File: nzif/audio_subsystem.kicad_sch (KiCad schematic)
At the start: 24 parts, among them U1201 ADAU1361, U1202 SSM2211S

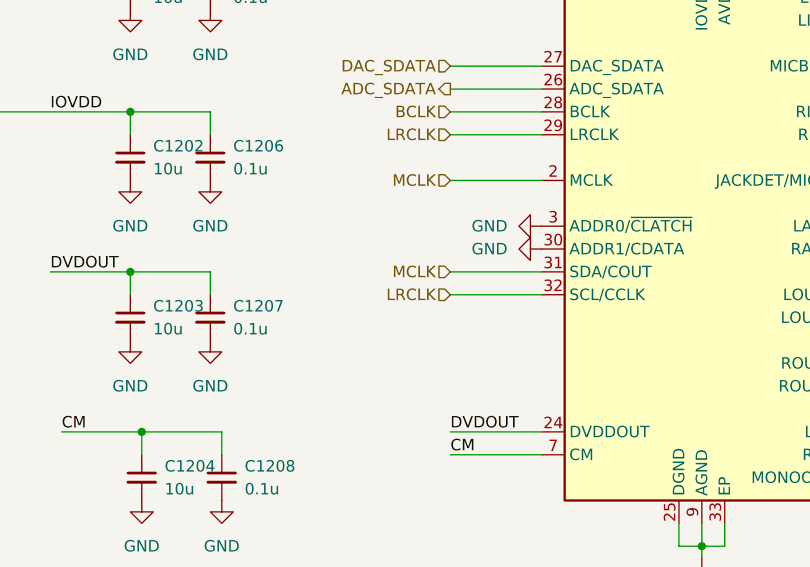
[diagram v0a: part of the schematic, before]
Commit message: top sheet wiring
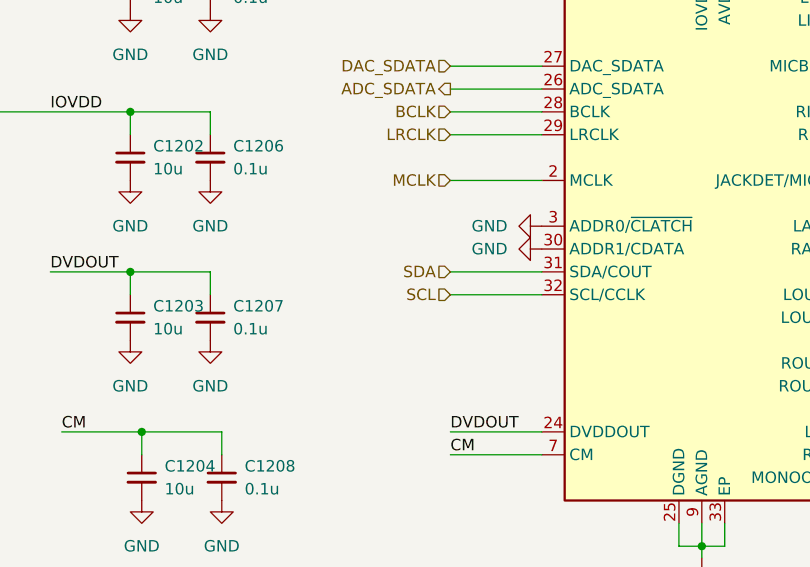
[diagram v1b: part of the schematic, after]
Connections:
- net LRCLK: no longer U1201.32 (SCL/CCLK)
- net MCLK: no longer U1201.31 (SDA/COUT)
- new net SCL: U1201.32 (SCL/CCLK)
- new net SDA: U1201.31 (SDA/COUT)
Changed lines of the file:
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@@
 		)
 	)
-	(hierarchical_label "MCLK"
+	(hierarchical_label "SDA"
 		(shape input)
 		(at 173.99 109.22 180)
@@
 		)
 	)
-	(hierarchical_label "LRCLK"
+	(hierarchical_label "SCL"
 		(shape input)
 		(at 173.99 111.76 180)

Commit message: updated top level
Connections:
- net LOUTN: now also U1201.18 (LOUTP)
- net at C1212.1: no longer U1201.21 (MONOOUT)
- net LOUTP: now reaches U1201.17 (LOUTN)
- net Line_Input_ROUTN: no longer names the net of U1201.16 (ROUTN)
- net Line_Input_ROUTP: no longer names the net of U1201.15 (ROUTP)
- no-connect marks 6 -> 7
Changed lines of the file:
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@@
+	)
+	(junction
+		(at 275.59 81.28)
+		(diameter 0)
+		(color 0 0 0 0)
 	)
 	(junction
@@
 	)
 	(no_connect
+		(at 219.71 121.92)
+	)
+	(no_connect
 		(at 219.71 93.98)
 	)
 	(no_connect
-		(at 219.71 114.3)
+		(at 219.71 132.08)
 	)
 	(no_connect
@@
 	)
 	(no_connect
+		(at 219.71 119.38)
+	)
+	(no_connect
 		(at 219.71 91.44)
 	)
-	(no_connect
-		(at 219.71 111.76)
+	(wire
+		(pts
+			(xy 215.9 180.34) (xy 224.79 180.34)
+		)
+		(stroke
+			(width 0)
+			(type default)
+		)
 	)
 	(wire
@@
 	(wire
 		(pts
-			(xy 219.71 132.08) (xy 227.33 132.08)
-		)
-		(stroke
-			(width 0)
-			(type default)
-		)
-	)
-	(wire
-		(pts
 			(xy 250.19 81.28) (xy 254 81.28)
 		)
@@
 	(wire
 		(pts
-			(xy 219.71 119.38) (xy 224.79 119.38)
+			(xy 219.71 111.76) (xy 228.6 111.76)
 		)
 		(stroke
@@
 	(wire
 		(pts
+			(xy 275.59 81.28) (xy 279.4 81.28)
+		)
+		(stroke
+			(width 0)
+			(type default)
+		)
+	)
+	(wire
+		(pts
+			(xy 215.9 182.88) (xy 224.79 182.88)
+		)
+		(stroke
+			(width 0)
+			(type default)
+		)
+	)
+	(wire
+		(pts
 			(xy 173.99 127) (xy 184.15 127)
 		)
@@
 	(wire
 		(pts
-			(xy 269.24 81.28) (xy 279.4 81.28)
+			(xy 269.24 81.28) (xy 275.59 81.28)
 		)
 		(stroke
@@
 	(wire
 		(pts
-			(xy 227.33 132.08) (xy 227.33 175.26)
-		)
-		(stroke
-			(width 0)
-			(type default)
-		)
-	)
-	(wire
-		(pts
 			(xy 173.99 99.06) (xy 184.15 99.06)
 		)
@@
 	(wire
 		(pts
+			(xy 275.59 76.2) (xy 275.59 81.28)
+		)
+		(stroke
+			(width 0)
+			(type default)
+		)
+	)
+	(wire
+		(pts
 			(xy 173.99 88.9) (xy 184.15 88.9)
 		)
@@
 	(wire
 		(pts
+			(xy 219.71 114.3) (xy 228.6 114.3)
+		)
+		(stroke
+			(width 0)
+			(type default)
+		)
+	)
+	(wire
+		(pts
 			(xy 147.32 93.98) (xy 147.32 91.44)
 		)
@@
 	(wire
 		(pts
-			(xy 219.71 121.92) (xy 224.79 121.92)
-		)
-		(stroke
-			(width 0)
-			(type default)
-		)
-	)
-	(wire
-		(pts
 			(xy 204.47 67.31) (xy 204.47 73.66)
 		)
@@
 	(wire
 		(pts
+			(xy 279.4 76.2) (xy 275.59 76.2)
+		)
+		(stroke
+			(width 0)
+			(type default)
+		)
+	)
+	(wire
+		(pts
 			(xy 254 81.28) (xy 254 83.82)
 		)
@@
 			(width 0)
 			(type default)
+		)
+	)
+	(label "LOUTP"
+		(at 228.6 114.3 180)
+		(effects
+			(font
+				(size 1.27 1.27)
+			)
+			(justify right bottom)
 		)
 	)
@@
 		)
 	)
+	(label "LOUTP"
+		(at 224.79 182.88 180)
+		(effects
+			(font
+				(size 1.27 1.27)
+			)
+			(justify right bottom)
+		)
+	)
 	(label "MICBIAS"
 		(at 232.41 73.66 0)
@@
 		)
 	)
+	(label "LOUTN"
+		(at 228.6 111.76 180)
+		(effects
+			(font
+				(size 1.27 1.27)
+			)
+			(justify right bottom)
+		)
+	)
 	(label "CM"
 		(at 130.81 127 0)
@@
 		)
 	)
+	(label "LOUTN"
+		(at 224.79 180.34 180)
+		(effects
+			(font
+				(size 1.27 1.27)
+			)
+			(justify right bottom)
+		)
+	)
 	(label "DVDOUT"
 		(at 173.99 127 0)
@@
 			)
 			(justify left bottom)
-		)
-	)
-	(label "LOUTN"
-		(at 231.14 114.3 180)
-		(effects
-			(font
-				(size 1.27 1.27)
-			)
-			(justify right bottom)
 		)
 	)
@@
 		)
 	)
-	(hierarchical_label "Line_Input_ROUTP"
-		(shape output)
-		(at 224.79 119.38 0)
-		(effects
-			(font
-				(size 1.27 1.27)
-			)
-			(justify left)
-		)
-	)
-	(hierarchical_label "Line_Input_ROUTN"
-		(shape output)
-		(at 224.79 121.92 0)
-		(effects
-			(font
-				(size 1.27 1.27)
-			)
-			(justify left)
-		)
-	)
 	(hierarchical_label "Headphone_L"
 		(shape input)
@@
 		)
 	)
+	(hierarchical_label "MIC_IN_EXT"
+		(shape input)
+		(at 279.4 76.2 0)
+		(effects
+			(font
+				(size 1.27 1.27)
+			)
+			(justify left)
+		)
+	)

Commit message: updates to top level
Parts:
- added R1216: 49.9, symbol Device:R_Small_US
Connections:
- net MCLK: now also R1216.1; no longer U1201.2 (MCLK)
- new net: R1216.2, U1201.2 (MCLK)
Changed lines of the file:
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@@
+	(wire
+		(pts
+			(xy 172.72 99.06) (xy 176.53 99.06)
+		)
+		(stroke
+			(width 0)
+			(type default)
+		)
+	)
 	(wire
 		(pts
@@
 	(wire
 		(pts
-			(xy 173.99 99.06) (xy 184.15 99.06)
-		)
-		(stroke
-			(width 0)
-			(type default)
-		)
-	)
-	(wire
-		(pts
 			(xy 251.46 175.26) (xy 256.54 175.26)
 		)
@@
 		(pts
 			(xy 292.1 182.88) (xy 313.69 182.88)
+		)
+		(stroke
+			(width 0)
+			(type default)
+		)
+	)
+	(wire
+		(pts
+			(xy 181.61 99.06) (xy 184.15 99.06)
 		)
 		(stroke
@@
 	(hierarchical_label "MCLK"
 		(shape input)
-		(at 173.99 99.06 180)
+		(at 172.72 99.06 180)
 		(effects
 			(font
@@
 					(unit 1)
 				)
+			)
+		)
+	)
+	(symbol
+		(lib_id "Device:R_Small_US")
+		(at 179.07 99.06 90)
+		(unit 1)
+		(body_style 1)
+		(exclude_from_sim no)
+		(in_bom yes)
+		(on_board yes)
+		(in_pos_files yes)
+		(dnp no)
+		(property "Reference" "R1216"
+			(at 173.99 97.282 90)
+			(show_name no)
+			(do_not_autoplace no)
+			(effects
+				(font
+					(size 1.27 1.27)
+				)
+			)
+		)
+		(property "Value" "49.9"
+			(at 181.102 97.028 90)
+			(show_name no)
+			(do_not_autoplace no)
+			(effects
+				(font
+					(size 1.27 1.27)
+				)
+			)
+		)
+		(property "Footprint" ""
+			(at 179.07 99.06 0)
+			(hide yes)
+			(show_name no)
+			(do_not_autoplace no)
+			(effects
+				(font
+					(size 1.27 1.27)
+				)
+			)
+		)
+		(property "Datasheet" ""
+			(at 179.07 99.06 0)
+			(hide yes)
+			(show_name no)
+			(do_not_autoplace no)
+			(effects
+				(font
+					(size 1.27 1.27)
+				)
+			)
+		)
+		(property "Description" "Resistor, small US symbol"
+			(at 179.07 99.06 0)
+			(hide yes)
+			(show_name no)
+			(do_not_autoplace no)
+			(effects
+				(font
+					(size 1.27 1.27)
+				)
+			)
+		)
+		(pin "1"
+		)
+		(pin "2"
+		)
+		(instances
+			(project "nzif"
+				(path "/fe42ca2f-2bb8-4d5a-9e84-807788ed632f/91ace161-62c2-4ad0-a80e-f8c3c9bc5e50"
+					(reference "R1216")
+					(unit 1)
+				)

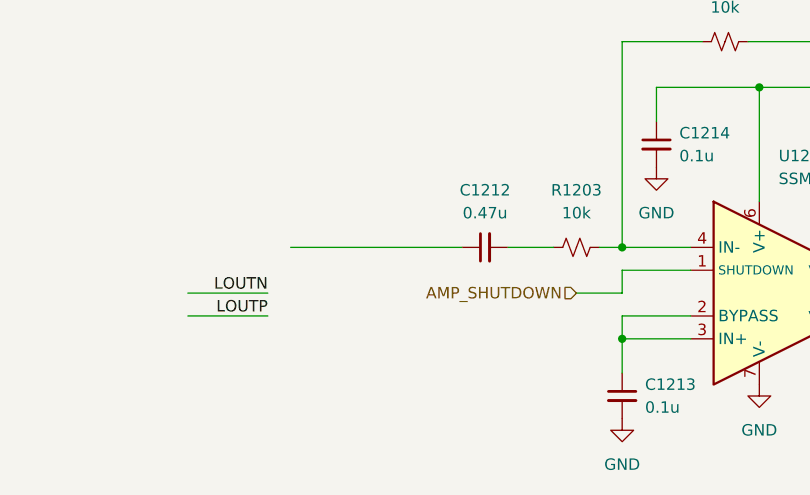
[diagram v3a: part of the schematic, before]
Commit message: Fix ERC errors: symbol pin types and schematic corrections
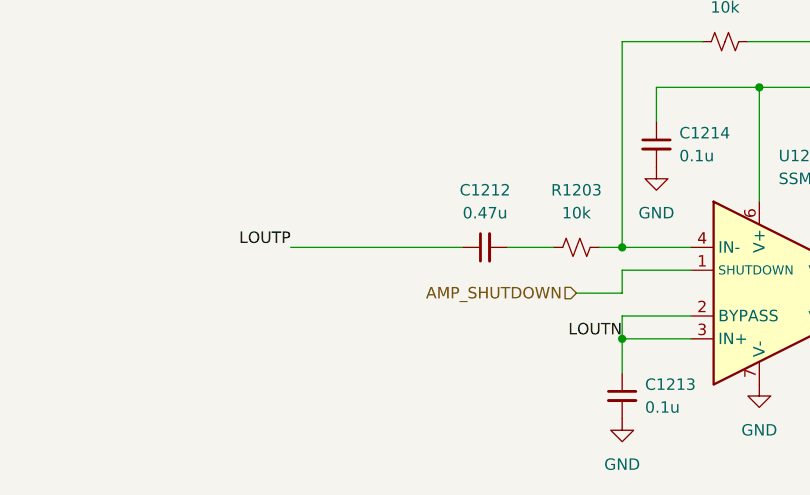
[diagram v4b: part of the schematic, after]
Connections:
- net LOUTN: now also C1213.1, U1202.2 (BYPASS), U1202.3 (IN+)
- net LOUTP: now also C1212.1
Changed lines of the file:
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@@
-	(wire
-		(pts
-			(xy 215.9 180.34) (xy 224.79 180.34)
-		)
-		(stroke
-			(width 0)
-			(type default)
-		)
-	)
 	(wire
 		(pts
@@
 		(pts
 			(xy 275.59 81.28) (xy 279.4 81.28)
-		)
-		(stroke
-			(width 0)
-			(type default)
-		)
-	)
-	(wire
-		(pts
-			(xy 215.9 182.88) (xy 224.79 182.88)
 		)
 		(stroke
@@
 	)
 	(label "LOUTP"
-		(at 224.79 182.88 180)
+		(at 227.33 175.26 180)
 		(effects
 			(font
@@
 	)
 	(label "LOUTN"
-		(at 224.79 180.34 180)
-		(effects
-			(font
+		(at 264.16 185.42 180)
+		(effects
+			(font

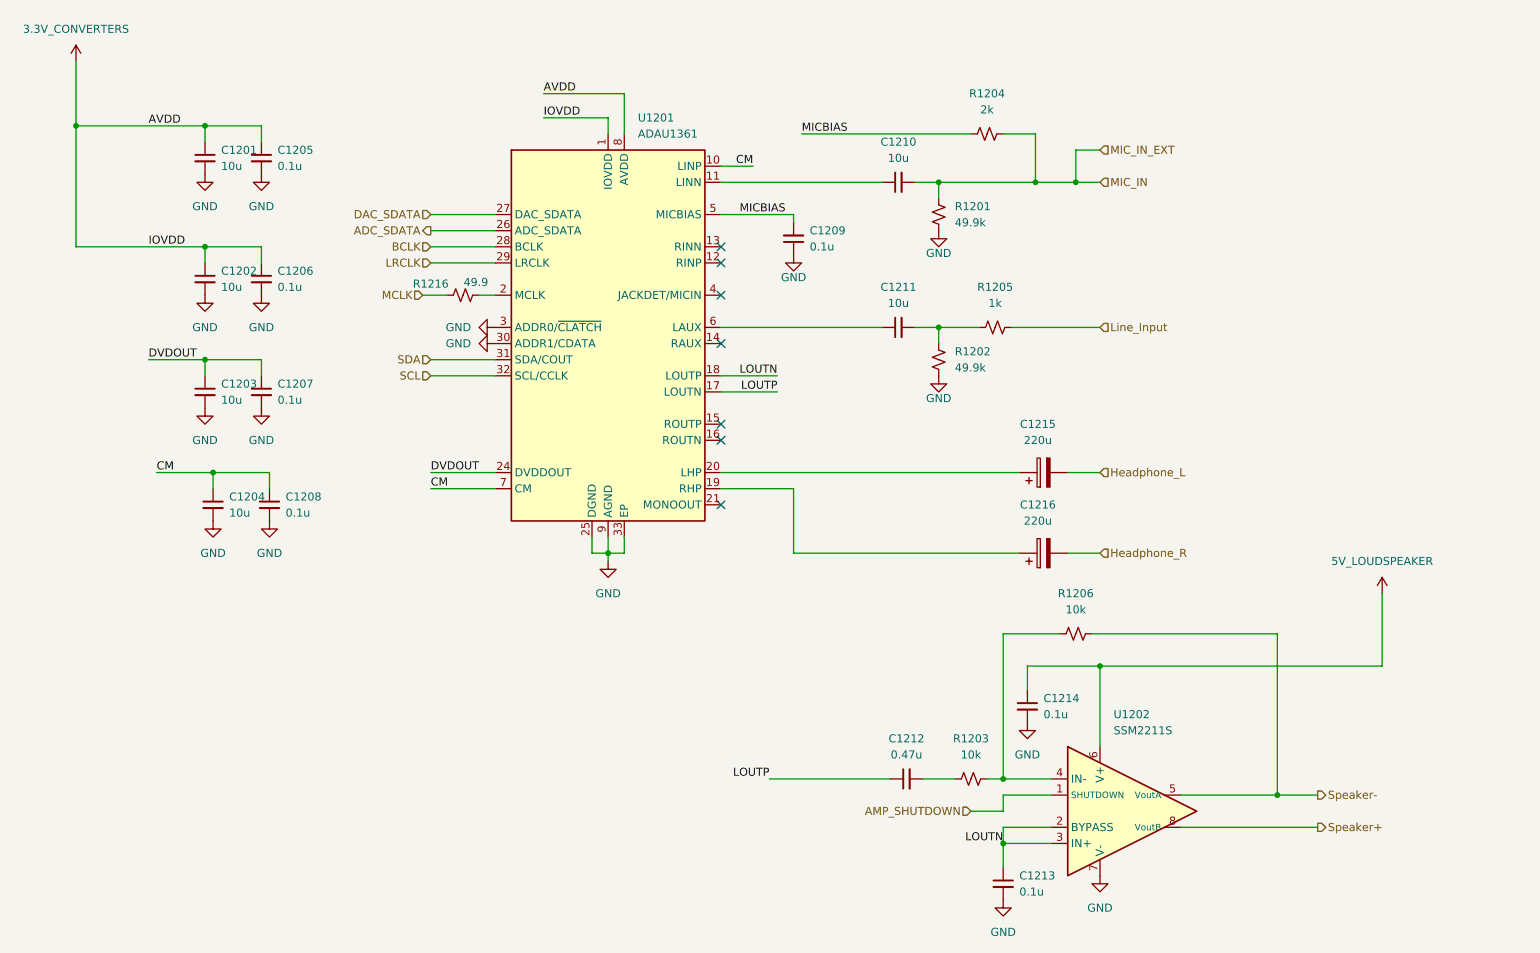
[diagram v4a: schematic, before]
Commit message: fixed minor erc related issues
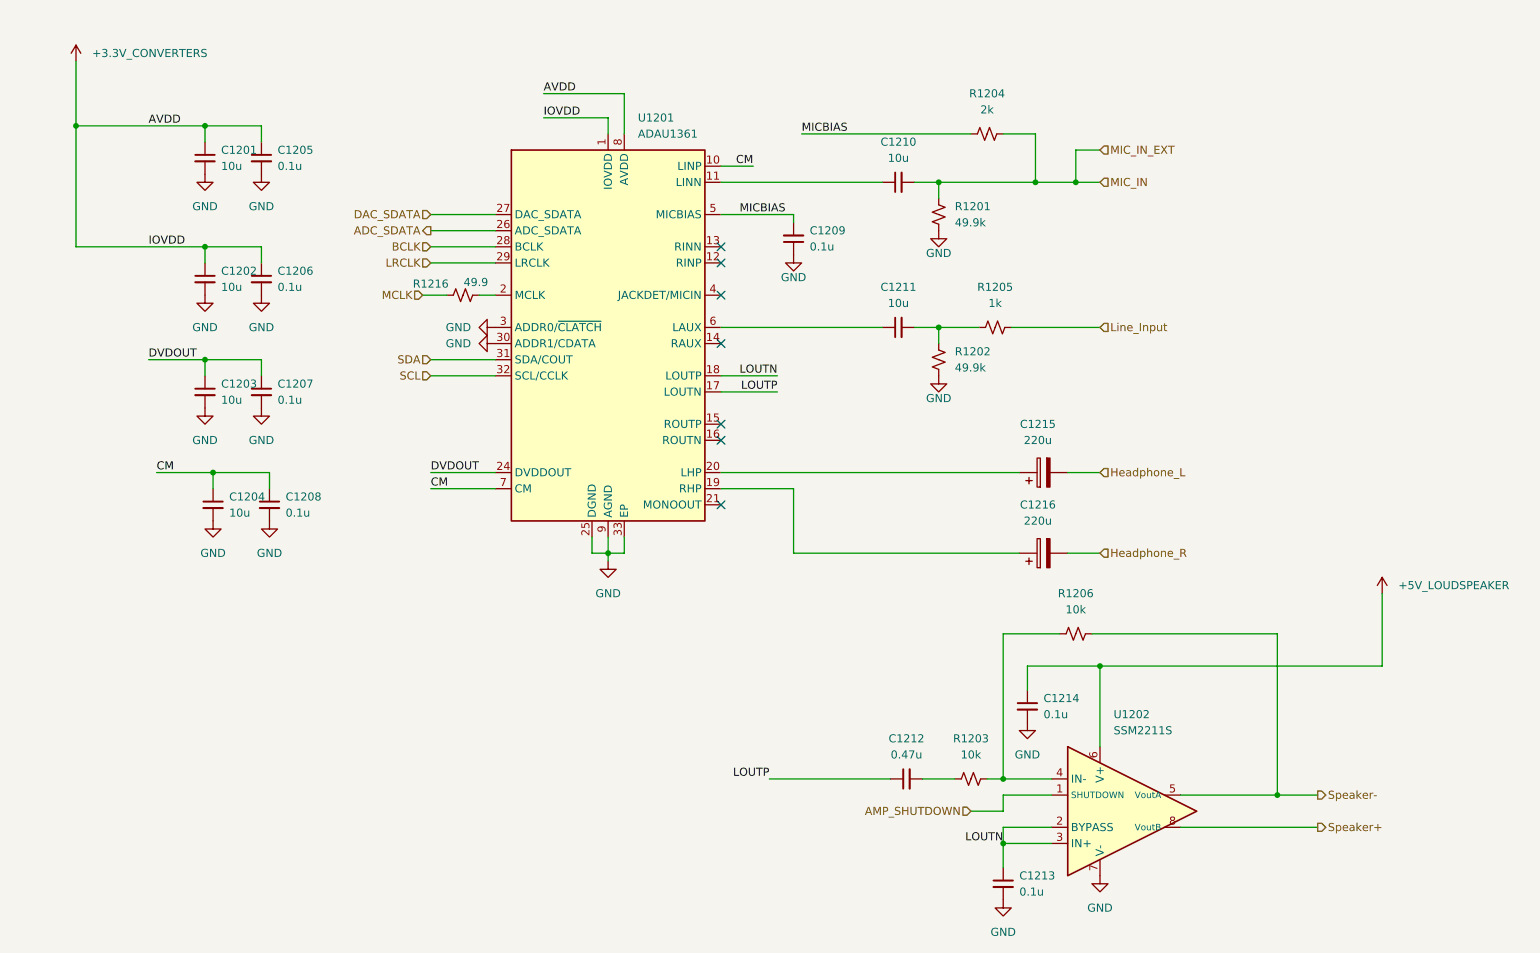
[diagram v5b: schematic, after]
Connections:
- net 3.3V_CONVERTERS renamed +3.3V_CONVERTERS
- net 5V_LOUDSPEAKER renamed +5V_LOUDSPEAKER
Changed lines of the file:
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@@
 			)
 		)
-		(property "Value" "5V_LOUDSPEAKER"
-			(at 323.85 140.97 0)
-			(show_name no)
-			(do_not_autoplace no)
-			(effects
-				(font
-					(size 1.27 1.27)
-				)
+		(property "Value" "+5V_LOUDSPEAKER"
+			(at 326.39 144.7799 0)
+			(show_name no)
+			(do_not_autoplace no)
+			(effects
+				(font
+					(size 1.27 1.27)
+				)
+				(justify left)
 			)
 		)
@@
 			)
 		)
-		(property "Value" "3.3V_CONVERTERS"
-			(at 118.11 57.15 0)
-			(show_name no)
-			(do_not_autoplace no)
-			(effects
-				(font
-					(size 1.27 1.27)
-				)
-			)
-		)
+		(property "Value" "+3.3V_CONVERTERS"
+			(at 120.65 60.9599 0)
+			(show_name no)
+			(do_not_autoplace no)
+			(effects
+				(font
+					(size 1.27 1.27)
+				)
+				(justify left)
+			)
+		)

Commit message: erc improvements
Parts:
- added R1229: 0, symbol Device:R_Small_US
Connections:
- net MIC_IN: now also R1229.1
- new net MIC_IN_EXT: R1229.2
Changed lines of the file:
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@@
+	(wire
+		(pts
+			(xy 288.29 76.2) (xy 292.1 76.2)
+		)
+		(stroke
+			(width 0)
+			(type default)
+		)
+	)
 	(wire
 		(pts
@@
 	(wire
 		(pts
-			(xy 279.4 76.2) (xy 275.59 76.2)
+			(xy 275.59 76.2) (xy 283.21 76.2)
 		)
 		(stroke
@@
 	(hierarchical_label "MIC_IN_EXT"
 		(shape input)
-		(at 279.4 76.2 0)
+		(at 292.1 76.2 0)
 		(effects
 			(font
@@
 					(unit 1)
 				)
+			)
+		)
+	)
+	(symbol
+		(lib_id "Device:R_Small_US")
+		(at 285.75 76.2 90)
+		(unit 1)
+		(body_style 1)
+		(exclude_from_sim yes)
+		(in_bom yes)
+		(on_board yes)
+		(in_pos_files yes)
+		(dnp no)
+		(fields_autoplaced yes)
+		(property "Reference" "R1229"
+			(at 285.75 69.85 90)
+			(show_name no)
+			(do_not_autoplace no)
+			(effects
+				(font
+					(size 1.27 1.27)
+				)
+			)
+		)
+		(property "Value" "0"
+			(at 285.75 72.39 90)
+			(show_name no)
+			(do_not_autoplace no)
+			(effects
+				(font
+					(size 1.27 1.27)
+				)
+			)
+		)
+		(property "Footprint" ""
+			(at 285.75 76.2 0)
+			(hide yes)
+			(show_name no)
+			(do_not_autoplace no)
+			(effects
+				(font
+					(size 1.27 1.27)
+				)
+			)
+		)
+		(property "Datasheet" ""
+			(at 285.75 76.2 0)
+			(hide yes)
+			(show_name no)
+			(do_not_autoplace no)
+			(effects
+				(font
+					(size 1.27 1.27)
+				)
+			)
+		)
+		(property "Description" "Resistor, small US symbol"
+			(at 285.75 76.2 0)
+			(hide yes)
+			(show_name no)
+			(do_not_autoplace no)
+			(effects
+				(font
+					(size 1.27 1.27)
+				)
+			)
+		)
+		(property "Digikey Part #" ""
+			(at 285.75 76.2 90)
+			(hide yes)
+			(show_name no)
+			(do_not_autoplace no)
+			(effects
+				(font
+					(size 1.27 1.27)
+				)
+			)
+		)
+		(pin "1"
+		)
+		(pin "2"
+		)
+		(instances
+			(project "nzif"
+				(path "/fe42ca2f-2bb8-4d5a-9e84-807788ed632f/91ace161-62c2-4ad0-a80e-f8c3c9bc5e50"
+					(reference "R1229")
+					(unit 1)
+				)

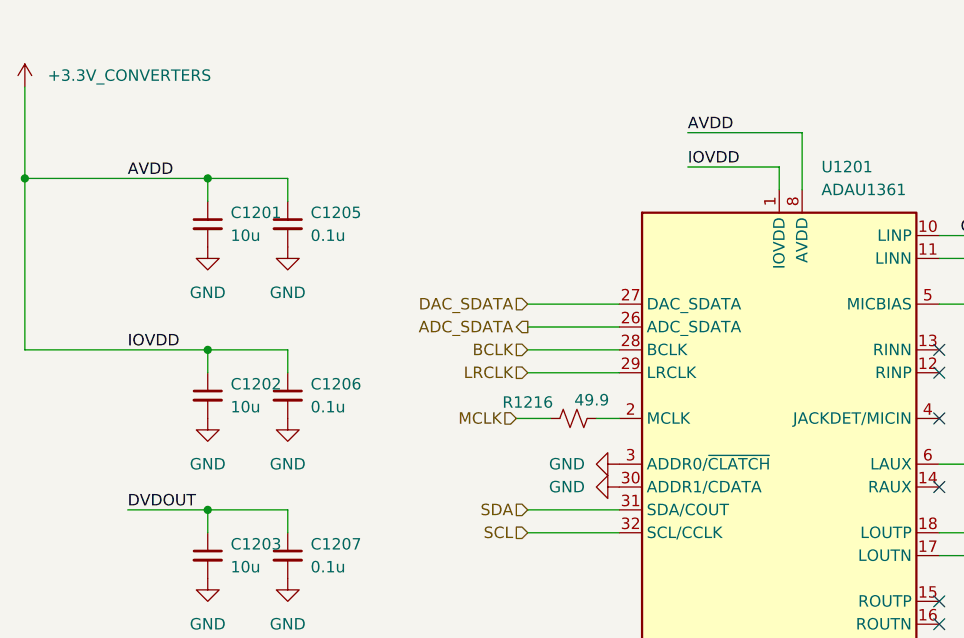
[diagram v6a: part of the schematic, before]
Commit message: fixed dvdd connection error
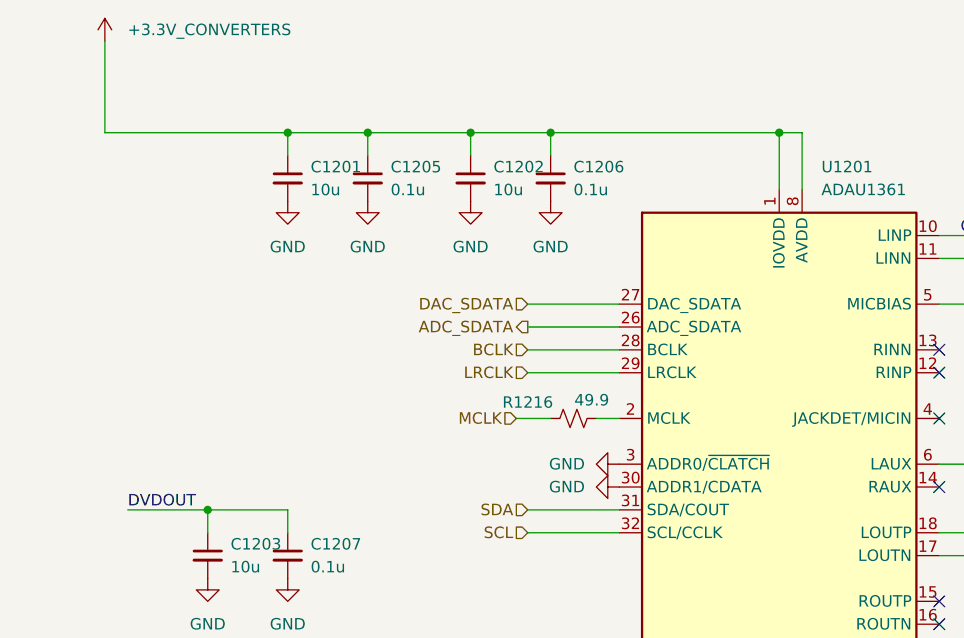
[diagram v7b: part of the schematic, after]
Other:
- moved on the sheet: C1201, C1202, C1205, C1206
